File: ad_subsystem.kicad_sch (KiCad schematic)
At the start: 8 parts, among them U3 CD4051B, U4 AD8603, U5 ADS7056IRUGR

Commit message: Add LCSC part numbers and fix C102 footprint
Add a hidden LCSC field to 290 symbols from the JLCPCB parts match
(2026-10-23). Left without LCSC: U7, U15, L1 (not in the JLCPCB
library), C1/C2/C4 and L2-L5 (no value specified), J3 (no confident
match) and Y3 (the 12 pF Basic crystal does not suit the 27 pF load
caps). U2, U12, Y2 and J9 carry the exact-MPN LCSC numbers although
they currently show zero JLCPCB stock.

C102 (22U 6V3) had a 0201 footprint; no 22 uF 0201 part exists. Change
it to 0402 (C415703) like C5-C7.
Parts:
- C3: LCSC (none) -> C1523
- R3: LCSC (none) -> C25077
- U3: LCSC (none) -> C54587
- U4: LCSC (none) -> C14937
- U5: LCSC (none) -> C2669798
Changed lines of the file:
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@@
+			)
+		)
+		(property "LCSC" "C14937"
+			(at 130.81 91.44 0)
+			(hide yes)
+			(show_name no)
+			(do_not_autoplace no)
+			(effects
+				(font
+					(size 1.27 1.27)
+				)
 			)
 		)
@@
 			)
 		)
+		(property "LCSC" "C1523"
+			(at 160.9852 101.6 0)
+			(hide yes)
+			(show_name no)
+			(do_not_autoplace no)
+			(effects
+				(font
+					(size 1.27 1.27)
+				)
+			)
+		)
 		(property "Datasheet" ""
 			(at 160.02 97.79 0)
@@
 			)
 		)
+		(property "LCSC" "C25077"
+			(at 149.86 93.218 90)
+			(hide yes)
+			(show_name no)
+			(do_not_autoplace no)
+			(effects
+				(font
+					(size 1.27 1.27)
+				)
+			)
+		)
 		(property "Datasheet" ""
 			(at 149.86 91.44 0)
@@
 			)
 		)
+		(property "LCSC" "C54587"
+			(at 87.63 67.31 0)
+			(hide yes)
+			(show_name no)
+			(do_not_autoplace no)
+			(effects
+				(font
+					(size 1.27 1.27)
+				)
+			)
+		)
 		(property "Datasheet" "http://www.ti.com/lit/ds/symlink/cd4052b.pdf"
 			(at 91.948 88.9 0)
@@
 			(at 181.61 93.98 0)
 			(hide yes)
+			(show_name no)
+			(do_not_autoplace no)
+			(effects
+				(font
+					(size 1.27 1.27)
+				)
+			)
+		)
+		(property "LCSC" "C2669798"
+			(at 181.61 93.98 0)
+			(hide yes)

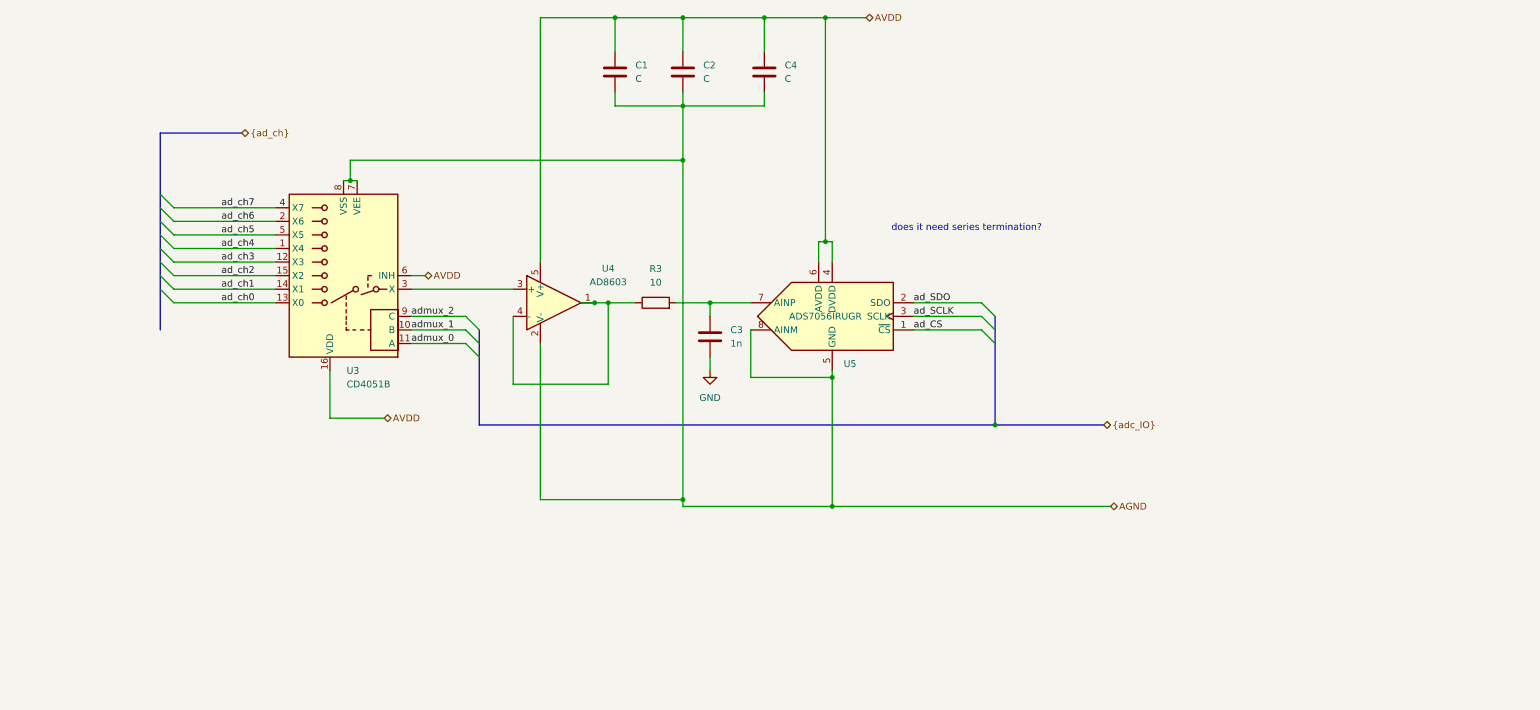
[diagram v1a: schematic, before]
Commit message: ADC: Agilex 3 card front end (mux enable fix, OPA365 driver, series R)
- U3 CD4051B -> SN74LV4051APWR (C7793), same pinout. Pin 6 (CD4051B
  INH, active high) was tied to AVDD, so all switches were always off.
  It is now tied to GND (LV4051 /E, active low).
- U4 AD8603 (0.4 MHz) -> OPA365AIDBVR (C96626, 50 MHz, same pinout,
  SOT-23-5). The ADS7056 kickback filter needs UGB >= 4/(2*pi*R*C).
- R3/C3 10R/1n -> 33R/680p NP0 (ADS7056 data sheet 9.2.1).
- C1/C2/C4: 4u7 0603 at AVDD (= reference), 100n, 100n; they had no
  values.
- U5 DVDD moves from AVDD to digital 3V3, with C261 1u.
- R265-R267 33R series on SDO/SCLK/CS.
Same front end as the Agilex 3 card and the Ti135 card.
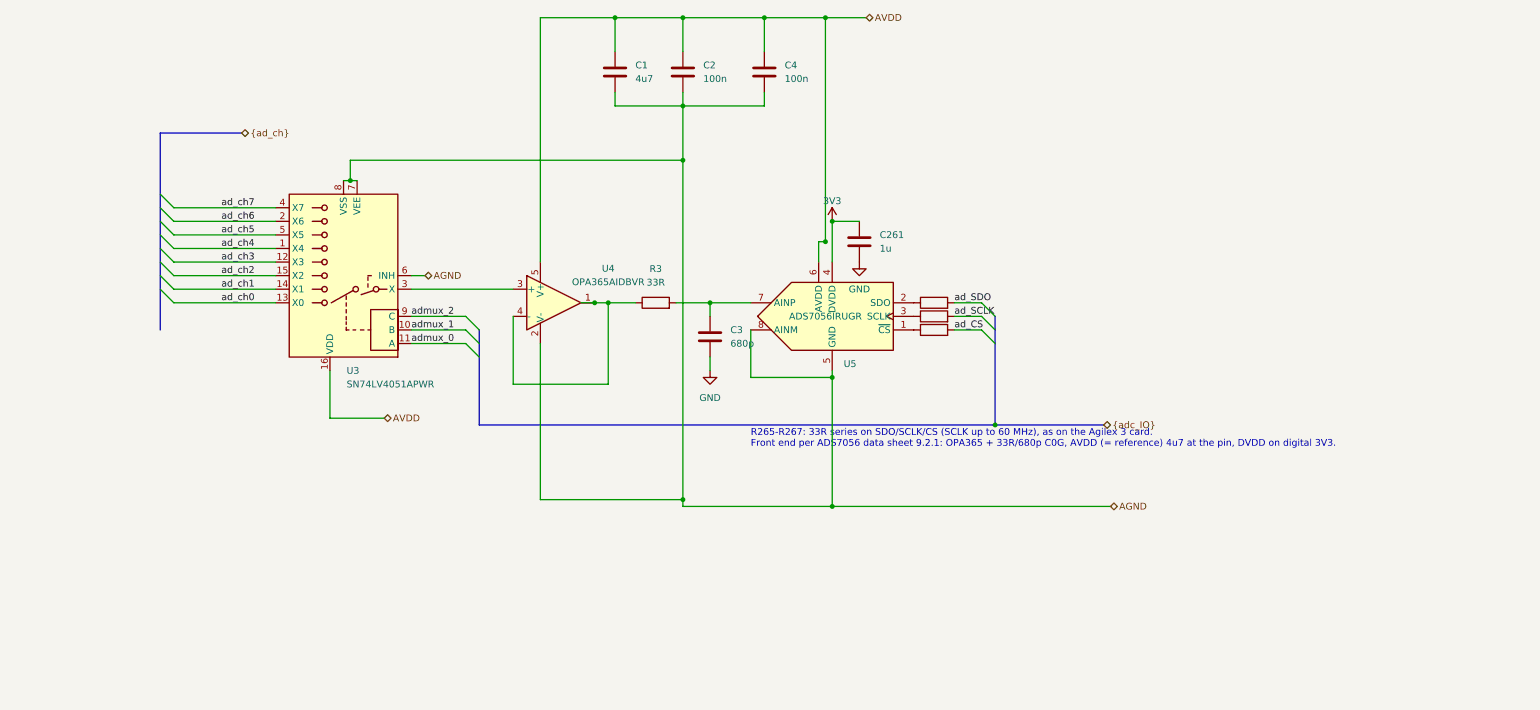
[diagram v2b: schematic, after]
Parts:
- added C261: 1u, Capacitor_SMD:C_0402_1005Metric, symbol Device:C
- added R265, R266, R267: 33R, Resistor_SMD:R_0402_1005Metric, symbol Device:R
- C1: value C -> 4u7; footprint Capacitor_SMD:C_0402_1005Metric -> Capacitor_SMD:C_0603_1608Metric; LCSC (none) -> C19666
- C2, C4: value C -> 100n; LCSC (none) -> C1525
- C3: value 1n -> 680p; LCSC C1523 -> C113781
- R3: value 10 -> 33R; LCSC C25077 -> C25105
- U3: value CD4051B -> SN74LV4051APWR; LCSC C54587 -> C7793
- U4: value AD8603 -> OPA365AIDBVR; footprint Package_TO_SOT_SMD:TSOT-23-5 -> Package_TO_SOT_SMD:SOT-23-5; LCSC C14937 -> C96626
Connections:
- net AGND: now also U3.6 (INH)
- net AVDD: no longer U3.6 (INH), U5.4 (DVDD)
- net GND: now also C261.2
- net ad_CS: now also R267.2; no longer U5.1 (~{CS})
- net ad_SCLK: now also R266.2; no longer U5.3 (SCLK)
- net ad_SDO: now also R265.2; no longer U5.2 (SDO)
- new net: R266.1, U5.3 (SCLK)
- new net: R267.1, U5.1 (~{CS})
- new net: R265.1, U5.2 (SDO)
- new net 3V3: C261.1, U5.4 (DVDD)
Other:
- note added: "R265-R267: 33R series on SDO/SCLK/CS (SCLK up to 60 MHz), as on the Agilex 3 card. Front end per ADS7056 data sheet 9.2.1: OPA365 + 33R/680p C0G, AVDD (= reference) 4u7 at the pin, DVDD on digital 3V3."
- note removed: "does it need series termination?"

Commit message: Schematic reorg step 1: remove dangling stubs and stale notes, correct notes, fill title blocks
Netlist: 0 renamed, 0 connectivity diffs; DRC parity 0. ERC 315 -> 242.
Plan refreshed for the eMMC, RTL8211FDI, TPS548A28 and the tuned LPDDR4 (IOBANK 3 sheet name kept).
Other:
- title: (none) -> ADC: input mux, buffer, ADS7056
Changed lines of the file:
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@@
 	(generator_version "10.0")
 	(paper "A4")
+	(title_block
+		(title "ADC: input mux, buffer, ADS7056")
+		(rev "${REVISION}")
+		(comment 1 "${BOARD}")
+	)
 	(text "R265-R267: 33R series on SDO/SCLK/CS (SCLK up to 60 MHz), as on the Agilex 3 card.\nFront end per ADS7056 data sheet 9.2.1: OPA365 + 33R/680p C0G, AVDD (= reference) 4u7 at the pin, DVDD on digital 3V3."
 		(exclude_from_sim no)

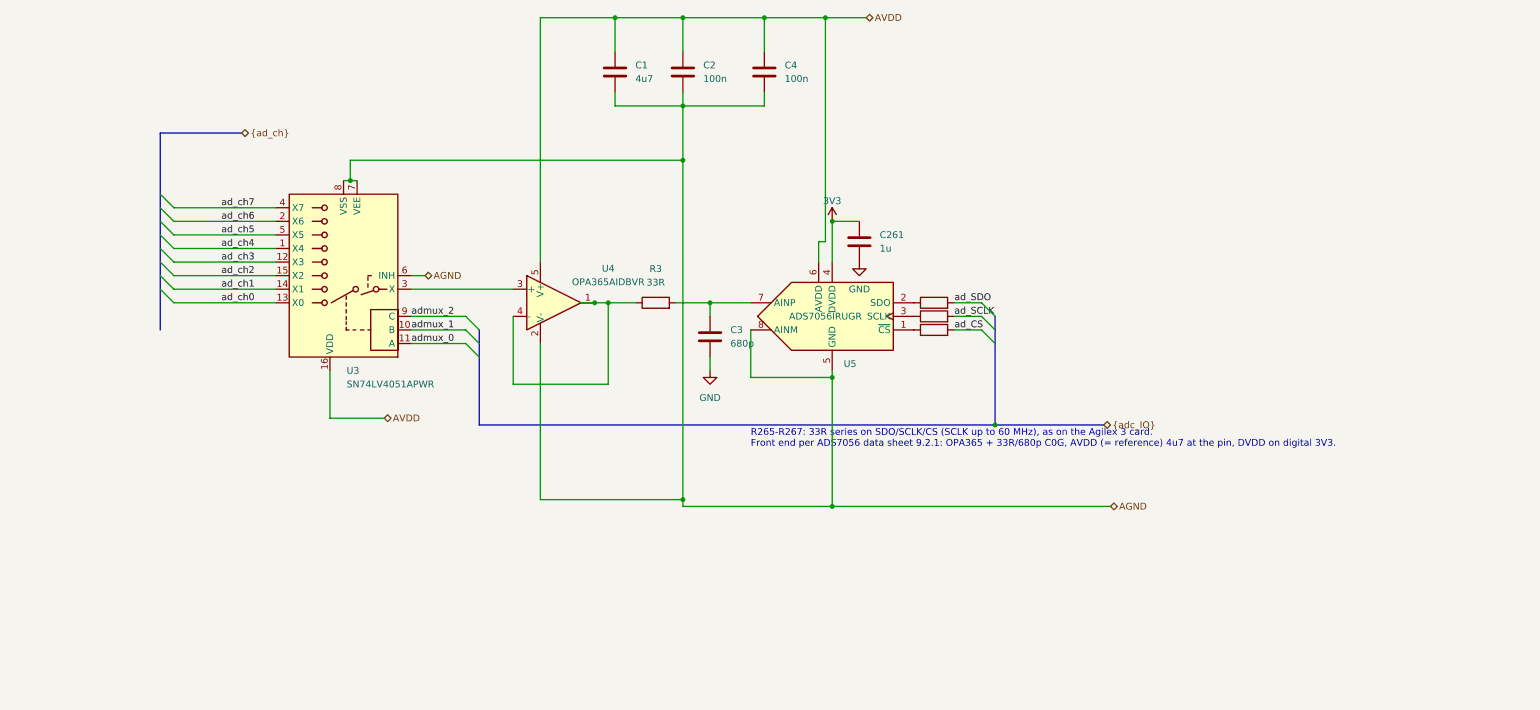
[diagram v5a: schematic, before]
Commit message: Schematic reorg step 3: U42 cluster on grid, U2 symbol redrawn, notes wrapped inside the frame
Netlist: 0 renamed, 0 connectivity diffs; DRC parity 0. ERC 223 -> 199 (no off-grid endpoints).
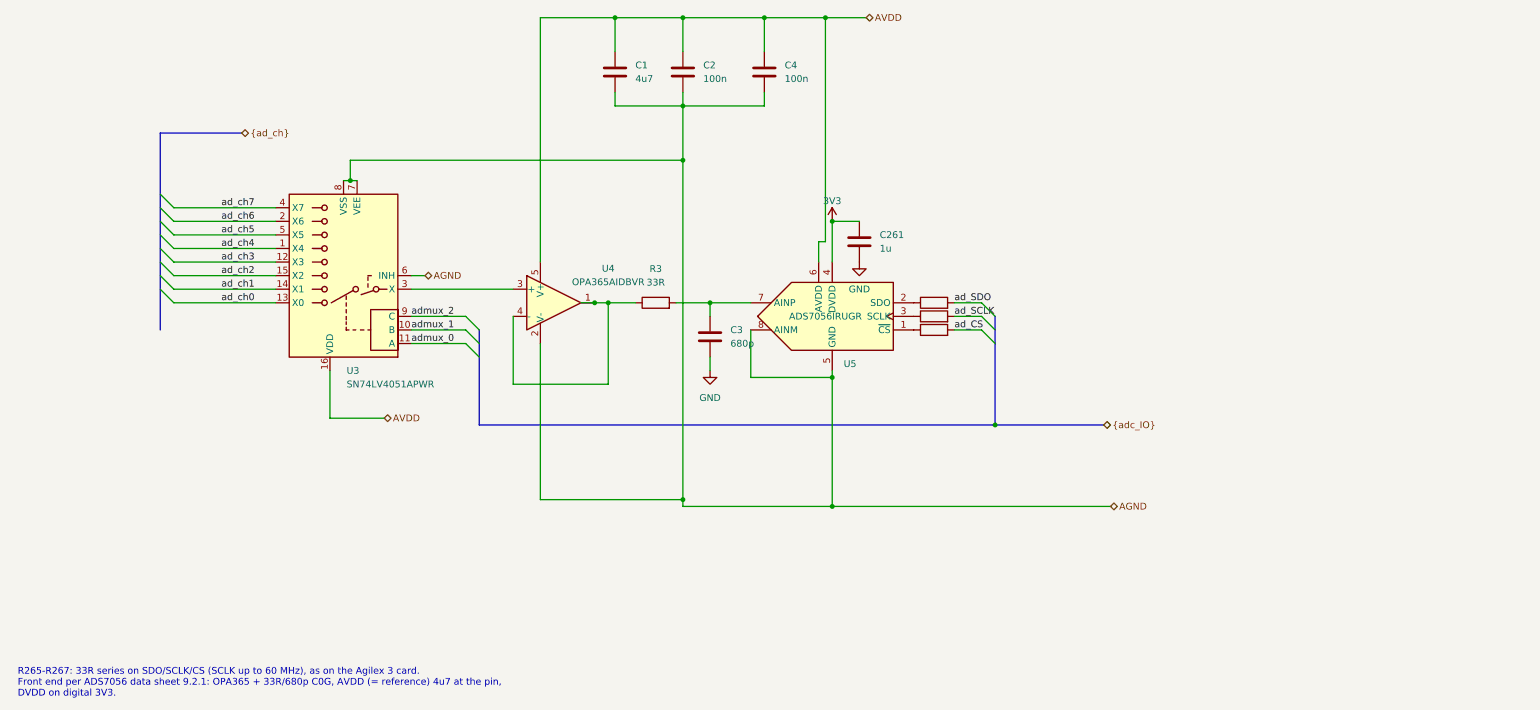
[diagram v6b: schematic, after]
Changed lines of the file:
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@@
 		(comment 1 "${BOARD}")
 	)
-	(text "R265-R267: 33R series on SDO/SCLK/CS (SCLK up to 60 MHz), as on the Agilex 3 card.\nFront end per ADS7056 data sheet 9.2.1: OPA365 + 33R/680p C0G, AVDD (= reference) 4u7 at the pin, DVDD on digital 3V3."
+	(text "R265-R267: 33R series on SDO/SCLK/CS (SCLK up to 60 MHz), as on the Agilex 3 card.\nFront end per ADS7056 data sheet 9.2.1: OPA365 + 33R/680p C0G, AVDD (= reference) 4u7 at the pin,\nDVDD on digital 3V3."
 		(exclude_from_sim no)
-		(at 167.64 116.84 0)
+		(at 30.48 162.56 0)
 		(effects
 			(font

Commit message: Schematic reorg step 5a: ADC rail-monitor dividers onto the ADC sheet
- R5, R42, R46, R51, R53, R54 and their rail symbols moved from the root to
  ad_subsystem (same symbol UUIDs); root bus branch to them removed
- Footprints re-linked to the ADC sheet path in the PCB
- R42/R51 footprint C_0402 -> R_0402 (they are 1k resistors); zones need a refill
- Note on the channel-to-rail mapping, sheet title updated

Netdiff: 0 renamed, 0 connectivity diffs. ERC 183. DRC parity 0.
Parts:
- added R42, R46, R51, R53, R54: 1k, Resistor_SMD:R_0402_1005Metric, symbol Device:R
- added R5: 100, Resistor_SMD:R_0402_1005Metric, symbol Device:R
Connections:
- net 3V3: now also R42.1
- net GND: now also R51.2
- net ad_ch0: now also R5.2
- net ad_ch1: now also R42.2, R51.1
- net ad_ch2: now also R53.2
- net ad_ch3: now also R54.2
- net ad_ch5: now also R46.2
- new net 1V1: R46.1
- new net 1V2: R54.1
- new net 1V8: R53.1
- new net VCORE: R5.1
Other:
- note added: "Rail monitor: ad_ch0 VCORE, ad_ch1 3V3 / 2, ad_ch2 1V8, ad_ch3 1V2, ad_ch5 1V1. ad_ch4, ad_ch6, ad_ch7 come from header J3."
- title: ADC: input mux, buffer, ADS7056 -> ADC: input mux, buffer, ADS7056, rail monitor

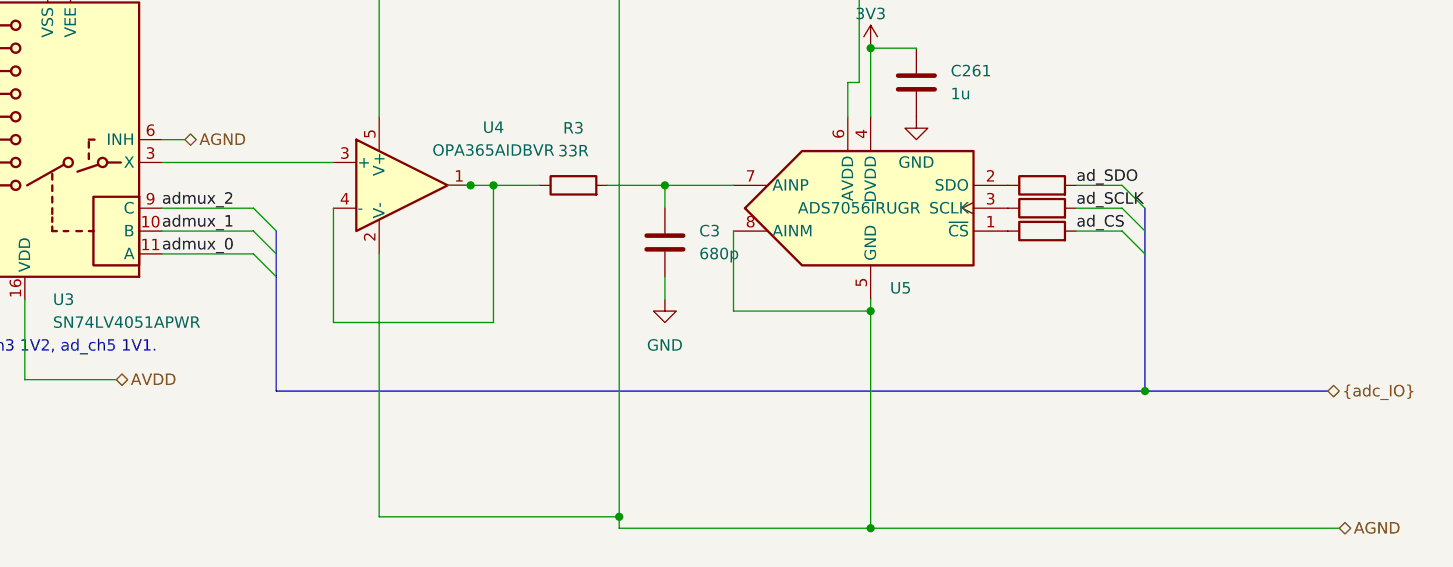
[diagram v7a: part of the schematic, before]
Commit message: Schematic reorg step 5e: one name per ADC wire
- ADC sheet exports adc_sdo, adc_sclk, adc_cs_n, adc_mux0..2 as single sheet
  pins instead of the {adc_IO} bus; each root wire keeps only its bank label,
  so the net names no longer change between edits
- Bus branch that tied the ADC wires to the {iob6b} bus removed

Netdiff: 0 renamed, 0 connectivity diffs. ERC 178 -> 157.
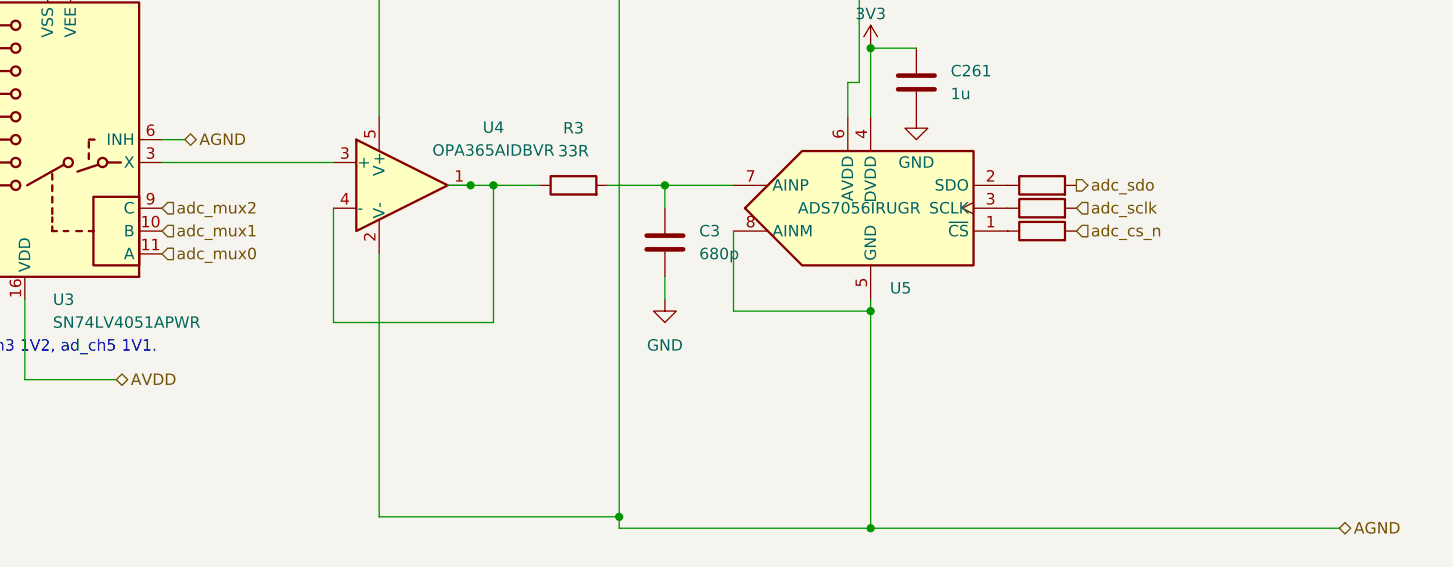
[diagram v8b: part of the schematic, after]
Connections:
- net ad_CS renamed adc_cs_n
- net ad_SCLK renamed adc_sclk
- net ad_SDO renamed adc_sdo
- net admux_0 renamed adc_mux0
- net admux_1 renamed adc_mux1
- net admux_2 renamed adc_mux2
